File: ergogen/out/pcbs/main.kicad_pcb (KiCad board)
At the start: 2 copper layers, 95 x 76 mm, 42 parts

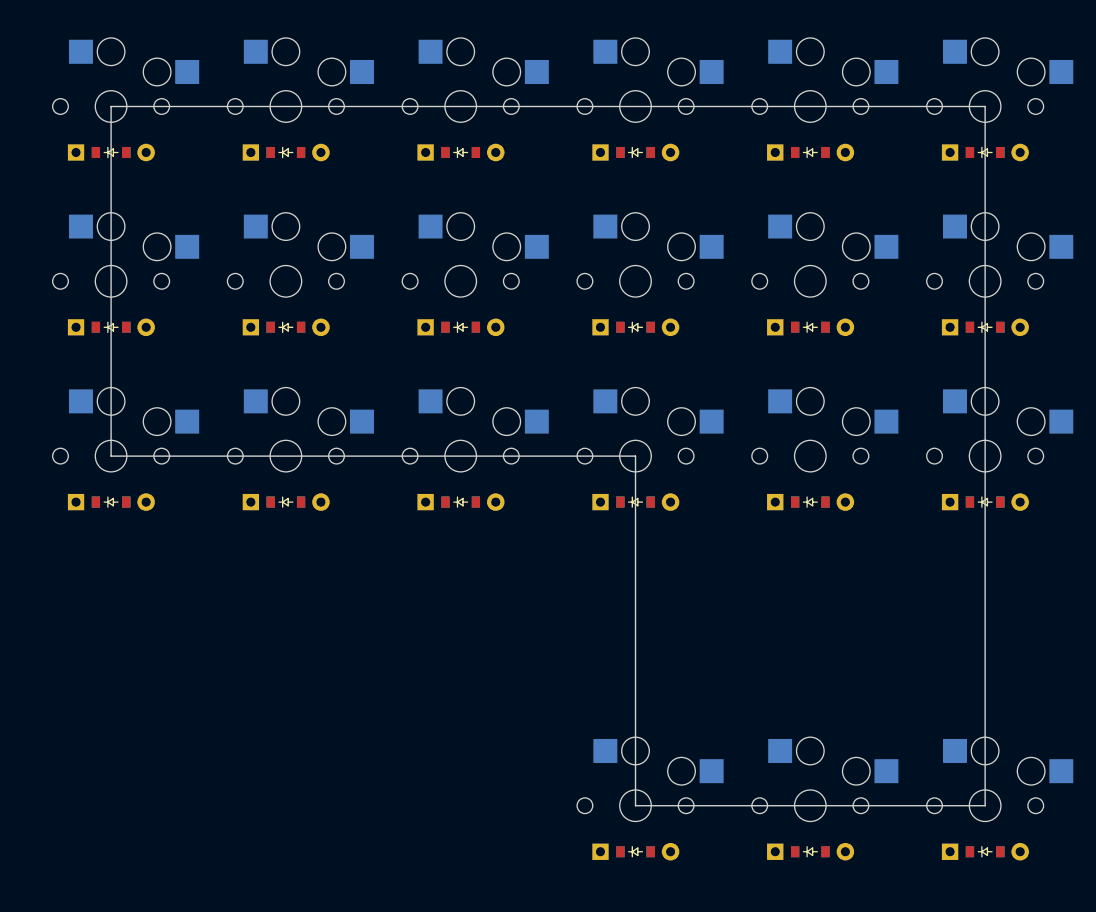
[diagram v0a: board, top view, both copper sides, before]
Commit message: feat: Improved outline padding.
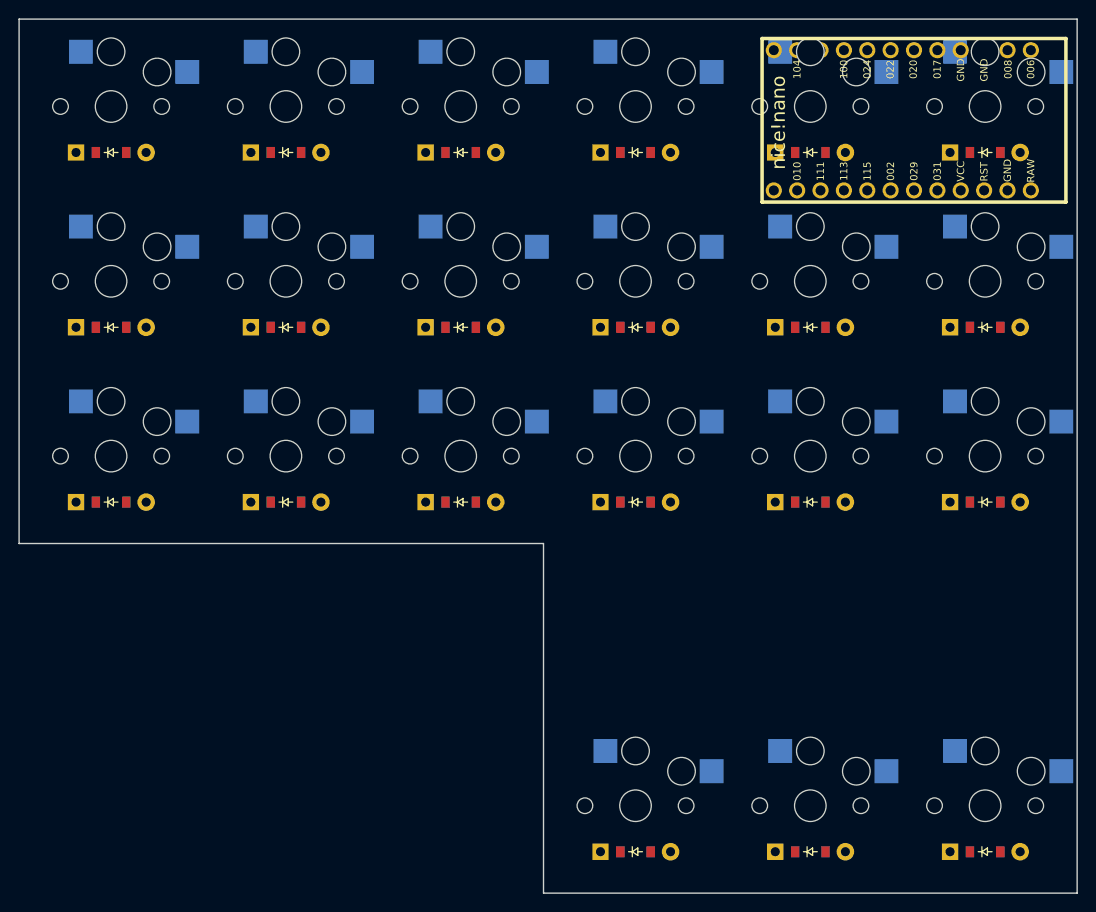
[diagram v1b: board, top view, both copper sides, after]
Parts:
- added MCU1: nice_nano, nice_nano, F.Cu at (86.0, -74.5)
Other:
- board size 95 x 76 mm -> 115 x 95 mm

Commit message: feat: Move diodes a little bit.
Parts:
- moved D1 2.00 mm to (2.00, -33.0)
- moved D10 2.00 mm to (59.0, 5.00)
- moved D11 2.00 mm to (59.0, -33.0)
- moved D12 2.00 mm to (59.0, -52.0)
- moved D13 2.00 mm to (59.0, -71.0)
- moved D14 2.00 mm to (78.0, 5.00)
- moved D15 2.00 mm to (78.0, -33.0)
- moved D16 2.00 mm to (78.0, -52.0)
- moved D17 2.00 mm to (78.0, -71.0)
- moved D18 2.00 mm to (97.0, 5.00)
- moved D19 2.00 mm to (97.0, -33.0)
- moved D2 2.00 mm to (2.00, -52.0)
- moved D20 2.00 mm to (97.0, -52.0)
- moved D21 2.00 mm to (97.0, -71.0)
- moved D3 2.00 mm to (2.00, -71.0)
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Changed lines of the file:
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@@
         )
     (module ComboDiode (layer F.Cu)
-        (at 0 -33 0)
+        (at 2 -33 0)
         (fp_text reference "D1" (at 0 0) (layer F.SilkS) hide (effects (font (size 1.27 1.27) (thickness 0.15))))
         (fp_text value "" (at 0 0) (layer F.SilkS) hide (effects (font (size 1.27 1.27) (thickness 0.15))))
@@
     )
     (module ComboDiode (layer F.Cu)
-        (at 0 -52 0)
+        (at 2 -52 0)
         (fp_text reference "D2" (at 0 0) (layer F.SilkS) hide (effects (font (size 1.27 1.27) (thickness 0.15))))
         (fp_text value "" (at 0 0) (layer F.SilkS) hide (effects (font (size 1.27 1.27) (thickness 0.15))))
@@
     )
     (module ComboDiode (layer F.Cu)
-        (at 0 -71 0)
+        (at 2 -71 0)
         (fp_text reference "D3" (at 0 0) (layer F.SilkS) hide (effects (font (size 1.27 1.27) (thickness 0.15))))
         (fp_text value "" (at 0 0) (layer F.SilkS) hide (effects (font (size 1.27 1.27) (thickness 0.15))))
@@
     )
     (module ComboDiode (layer F.Cu)
-        (at 19 -33 0)
+        (at 21 -33 0)
         (fp_text reference "D4" (at 0 0) (layer F.SilkS) hide (effects (font (size 1.27 1.27) (thickness 0.15))))
         (fp_text value "" (at 0 0) (layer F.SilkS) hide (effects (font (size 1.27 1.27) (thickness 0.15))))
@@
     )
     (module ComboDiode (layer F.Cu)
-        (at 19 -52 0)
+        (at 21 -52 0)
         (fp_text reference "D5" (at 0 0) (layer F.SilkS) hide (effects (font (size 1.27 1.27) (thickness 0.15))))
         (fp_text value "" (at 0 0) (layer F.SilkS) hide (effects (font (size 1.27 1.27) (thickness 0.15))))
@@
     )
     (module ComboDiode (layer F.Cu)
-        (at 19 -71 0)
+        (at 21 -71 0)
         (fp_text reference "D6" (at 0 0) (layer F.SilkS) hide (effects (font (size 1.27 1.27) (thickness 0.15))))
         (fp_text value "" (at 0 0) (layer F.SilkS) hide (effects (font (size 1.27 1.27) (thickness 0.15))))
@@
     )
     (module ComboDiode (layer F.Cu)
-        (at 38 -33 0)
+        (at 40 -33 0)
         (fp_text reference "D7" (at 0 0) (layer F.SilkS) hide (effects (font (size 1.27 1.27) (thickness 0.15))))
         (fp_text value "" (at 0 0) (layer F.SilkS) hide (effects (font (size 1.27 1.27) (thickness 0.15))))
@@
     )
     (module ComboDiode (layer F.Cu)
-        (at 38 -52 0)
+        (at 40 -52 0)
         (fp_text reference "D8" (at 0 0) (layer F.SilkS) hide (effects (font (size 1.27 1.27) (thickness 0.15))))
         (fp_text value "" (at 0 0) (layer F.SilkS) hide (effects (font (size 1.27 1.27) (thickness 0.15))))
@@
     )
     (module ComboDiode (layer F.Cu)
-        (at 38 -71 0)
+        (at 40 -71 0)
         (fp_text reference "D9" (at 0 0) (layer F.SilkS) hide (effects (font (size 1.27 1.27) (thickness 0.15))))
         (fp_text value "" (at 0 0) (layer F.SilkS) hide (effects (font (size 1.27 1.27) (thickness 0.15))))
@@
     )
     (module ComboDiode (layer F.Cu)
-        (at 57 5 0)
+        (at 59 5 0)
         (fp_text reference "D10" (at 0 0) (layer F.SilkS) hide (effects (font (size 1.27 1.27) (thickness 0.15))))
         (fp_text value "" (at 0 0) (layer F.SilkS) hide (effects (font (size 1.27 1.27) (thickness 0.15))))
@@
     )
     (module ComboDiode (layer F.Cu)
-        (at 57 -33 0)
+        (at 59 -33 0)
         (fp_text reference "D11" (at 0 0) (layer F.SilkS) hide (effects (font (size 1.27 1.27) (thickness 0.15))))
         (fp_text value "" (at 0 0) (layer F.SilkS) hide (effects (font (size 1.27 1.27) (thickness 0.15))))
@@
     )
     (module ComboDiode (layer F.Cu)
-        (at 57 -52 0)
+        (at 59 -52 0)
         (fp_text reference "D12" (at 0 0) (layer F.SilkS) hide (effects (font (size 1.27 1.27) (thickness 0.15))))
         (fp_text value "" (at 0 0) (layer F.SilkS) hide (effects (font (size 1.27 1.27) (thickness 0.15))))
@@
     )
     (module ComboDiode (layer F.Cu)
-        (at 57 -71 0)
+        (at 59 -71 0)
         (fp_text reference "D13" (at 0 0) (layer F.SilkS) hide (effects (font (size 1.27 1.27) (thickness 0.15))))
         (fp_text value "" (at 0 0) (layer F.SilkS) hide (effects (font (size 1.27 1.27) (thickness 0.15))))
@@
     )
     (module ComboDiode (layer F.Cu)
-        (at 76 5 0)
+        (at 78 5 0)
         (fp_text reference "D14" (at 0 0) (layer F.SilkS) hide (effects (font (size 1.27 1.27) (thickness 0.15))))
         (fp_text value "" (at 0 0) (layer F.SilkS) hide (effects (font (size 1.27 1.27) (thickness 0.15))))
@@
     )
     (module ComboDiode (layer F.Cu)
-        (at 76 -33 0)
+        (at 78 -33 0)
         (fp_text reference "D15" (at 0 0) (layer F.SilkS) hide (effects (font (size 1.27 1.27) (thickness 0.15))))
         (fp_text value "" (at 0 0) (layer F.SilkS) hide (effects (font (size 1.27 1.27) (thickness 0.15))))
@@
     )
     (module ComboDiode (layer F.Cu)
-        (at 76 -52 0)
+        (at 78 -52 0)
         (fp_text reference "D16" (at 0 0) (layer F.SilkS) hide (effects (font (size 1.27 1.27) (thickness 0.15))))
         (fp_text value "" (at 0 0) (layer F.SilkS) hide (effects (font (size 1.27 1.27) (thickness 0.15))))
@@
     )
     (module ComboDiode (layer F.Cu)
-        (at 76 -71 0)
+        (at 78 -71 0)
         (fp_text reference "D17" (at 0 0) (layer F.SilkS) hide (effects (font (size 1.27 1.27) (thickness 0.15))))
         (fp_text value "" (at 0 0) (layer F.SilkS) hide (effects (font (size 1.27 1.27) (thickness 0.15))))
@@
     )
     (module ComboDiode (layer F.Cu)
-        (at 95 5 0)
+        (at 97 5 0)
         (fp_text reference "D18" (at 0 0) (layer F.SilkS) hide (effects (font (size 1.27 1.27) (thickness 0.15))))
         (fp_text value "" (at 0 0) (layer F.SilkS) hide (effects (font (size 1.27 1.27) (thickness 0.15))))
@@
     )
     (module ComboDiode (layer F.Cu)
-        (at 95 -33 0)
+        (at 97 -33 0)
         (fp_text reference "D19" (at 0 0) (layer F.SilkS) hide (effects (font (size 1.27 1.27) (thickness 0.15))))
         (fp_text value "" (at 0 0) (layer F.SilkS) hide (effects (font (size 1.27 1.27) (thickness 0.15))))
@@
     )
     (module ComboDiode (layer F.Cu)
-        (at 95 -52 0)
+        (at 97 -52 0)
         (fp_text reference "D20" (at 0 0) (layer F.SilkS) hide (effects (font (size 1.27 1.27) (thickness 0.15))))
         (fp_text value "" (at 0 0) (layer F.SilkS) hide (effects (font (size 1.27 1.27) (thickness 0.15))))
@@
     )
     (module ComboDiode (layer F.Cu)
-        (at 95 -71 0)
+        (at 97 -71 0)
         (fp_text reference "D21" (at 0 0) (layer F.SilkS) hide (effects (font (size 1.27 1.27) (thickness 0.15))))
         (fp_text value "" (at 0 0) (layer F.SilkS) hide (effects (font (size 1.27 1.27) (thickness 0.15))))

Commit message: feat: Shift nice nano to the empty row.
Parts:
- moved MCU1 55.5 mm to (87.0, -19.0)

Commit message: feat: Add battery jack.
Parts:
- added JST1: , JST_PH_S2B-PH-K_02x2.00mm_Angled, F.Cu at (62.0, -23.0)
- moved MCU1 1.41 mm to (86.0, -18.0)
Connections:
- D1 pad 1: P002 -> P017
- D10 pad 1: P113 -> P010
- D11 pad 1: P002 -> P017
- D12 pad 1: P029 -> P020
- D13 pad 1: P031 -> P022
- D14 pad 1: P113 -> P010
- D15 pad 1: P002 -> P017
- D16 pad 1: P029 -> P020
- D17 pad 1: P031 -> P022
- D18 pad 1: P113 -> P010
- D19 pad 1: P002 -> P017
- D2 pad 1: P029 -> P020
- D20 pad 1: P029 -> P020
- D21 pad 1: P031 -> P022
- D3 pad 1: P031 -> P022
- D4 pad 1: P002 -> P017
- D5 pad 1: P029 -> P020
- D6 pad 1: P031 -> P022
- D7 pad 1: P002 -> P017
- D8 pad 1: P029 -> P020
- D9 pad 1: P031 -> P022
- S1 pad 1: P020 -> P031
- S10 pad 1: P100 -> P115
- S11 pad 1: P100 -> P115
- S12 pad 1: P100 -> P115
- S13 pad 1: P100 -> P115
- S14 pad 1: P011 -> P113
- S15 pad 1: P011 -> P113
- S16 pad 1: P011 -> P113
- S17 pad 1: P011 -> P113
- S18 pad 1: P017 -> P111
- S19 pad 1: P017 -> P111
- S2 pad 1: P020 -> P031
- S20 pad 1: P017 -> P111
- S21 pad 1: P017 -> P111
- S3 pad 1: P020 -> P031
- S4 pad 1: P022 -> P029
- S5 pad 1: P022 -> P029
- S6 pad 1: P022 -> P029
- S7 pad 1: P024 -> P002
- S8 pad 1: P024 -> P002
- S9 pad 1: P024 -> P002

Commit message: feat: Add reset switch.
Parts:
- added B1: Panasonic_EVQPUL_EVQPUC, Panasonic_EVQPUL_EVQPUC, F.Cu at (49.0, -16.0)
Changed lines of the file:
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@@
         (pad 2 thru_hole oval (at 1 0 -90) (size 1.2 1.7) (drill 0.75) (layers *.Cu *.Mask) (net 33 "GND"))
+    )
+    (module Panasonic_EVQPUL_EVQPUC (layer F.Cu)
+        (descr "http://industrial.panasonic.com/cdbs/www-data/pdf/ATV0000/ATV0000CE5.pdf")
+        (tags "SMD SMT SPST EVQPUL EVQPUC")
+        (at 49 -16 90)
+        (fp_text reference "B1" (at 0 0) (layer "F.SilkS") hide (effects (font (size 1 1) (thickness 0.15))))
+        (fp_text value "Panasonic_EVQPUL_EVQPUC" (at 0 3.5) (layer "F.Fab") hide (effects (font (size 1 1) (thickness 0.15))))
+        (fp_line (start -2.45 0.275) (end -2.45 -0.275) (stroke (width 0.12) (type solid)) (layer "B.SilkS"))
+        (fp_line (start -1.425 -1.85) (end -2.35 -1.85) (stroke (width 0.12) (type solid)) (layer "B.SilkS"))
+        (fp_line (start 2.35 -1.85) (end 1.425 -1.85) (stroke (width 0.12) (type solid)) (layer "B.SilkS"))
+        (fp_line (start 2.35 1.85) (end -2.35 1.85) (stroke (width 0.12) (type solid)) (layer "B.SilkS"))
+        (fp_line (start 2.45 0.275) (end 2.45 -0.275) (stroke (width 0.12) (type solid)) (layer "B.SilkS"))
+        (fp_line (start -3.9 2.25) (end -3.9 -3.25) (stroke (width 0.05) (type solid)) (layer "B.CrtYd"))
+        (fp_line (start 3.9 -3.25) (end -3.9 -3.25) (stroke (width 0.05) (type solid)) (layer "B.CrtYd"))
+        (fp_line (start 3.9 2.25) (end -3.9 2.25) (stroke (width 0.05) (type solid)) (layer "B.CrtYd"))
+        (fp_line (start 3.9 2.25) (end 3.9 -3.25) (stroke (width 0.05) (type solid)) (layer "B.CrtYd"))
+        (fp_line (start -2.35 1.75) (end -2.35 -1.75) (stroke (width 0.1) (type solid)) (layer "B.Fab"))
+        (fp_line (start -1.3 -2.75) (end -1.3 -1.75) (stroke (width 0.1) (type solid)) (layer "B.Fab"))
+        (fp_line (start 1.3 -2.75) (end -1.3 -2.75) (stroke (width 0.1) (type solid)) (layer "B.Fab"))
+        (fp_line (start 1.3 -2.75) (end 1.3 -1.75) (stroke (width 0.1) (type solid)) (layer "B.Fab"))
+        (fp_line (start 2.35 -1.75) (end -2.35 -1.75) (stroke (width 0.1) (type solid)) (layer "B.Fab"))
+        (fp_line (start 2.35 1.75) (end -2.35 1.75) (stroke (width 0.1) (type solid)) (layer "B.Fab"))
+        (fp_line (start 2.35 1.75) (end 2.35 -1.75) (stroke (width 0.1) (type solid)) (layer "B.Fab"))
+        (pad "" np_thru_hole circle (at 0 -1.375 90) (size 0.75 0.75) (drill 0.75) (layers "*.Cu" "*.Mask"))
+        (pad "" np_thru_hole circle (at 0 1.375 90) (size 0.75 0.75) (drill 0.75) (layers "*.Cu" "*.Mask"))
+        (pad "1" smd rect (at -2.625 -0.85 90) (size 1.55 1) (layers "B.Cu" "B.Paste" "B.Mask") (net 33 "GND"))
+        (pad "1" smd rect (at 2.625 -0.85 90) (size 1.55 1) (layers "B.Cu" "B.Paste" "B.Mask") (net 33 "GND"))
+        (pad "2" smd rect (at -2.625 0.85 90) (size 1.55 1) (layers "B.Cu" "B.Paste" "B.Mask") (net 34 "RST"))
+        (pad "2" smd rect (at 2.625 0.85 90) (size 1.55 1) (layers "B.Cu" "B.Paste" "B.Mask") (net 34 "RST"))
     )
   (gr_line (start -10 -85.5) (end 105 -85.5) (angle 90) (layer Edge.Cuts) (width 0.15))

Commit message: feat: Add battery switch
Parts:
- added T1: , E73:SPDT_C128955, F.Cu at (49.0, -24.0)
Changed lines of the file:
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@@
         (pad "2" smd rect (at 2.625 0.85 90) (size 1.55 1) (layers "B.Cu" "B.Paste" "B.Mask") (net 34 "RST"))
     )
+        (module E73:SPDT_C128955 (layer F.Cu)
+            (at 49 -24 90)
+            (fp_text reference "T1" (at 0 0) (layer F.SilkS) hide (effects (font (size 1.27 1.27) (thickness 0.15))))
+            (fp_text value "" (at 0 0) (layer F.SilkS) hide (effects (font (size 1.27 1.27) (thickness 0.15))))
+            (fp_line (start 1.95 -1.35) (end -1.95 -1.35) (layer B.SilkS) (width 0.15))
+            (fp_line (start 0 -1.35) (end -3.3 -1.35) (layer B.SilkS) (width 0.15))
+            (fp_line (start -3.3 -1.35) (end -3.3 1.5) (layer B.SilkS) (width 0.15))
+            (fp_line (start -3.3 1.5) (end 3.3 1.5) (layer B.SilkS) (width 0.15))
+            (fp_line (start 3.3 1.5) (end 3.3 -1.35) (layer B.SilkS) (width 0.15))
+            (fp_line (start 0 -1.35) (end 3.3 -1.35) (layer B.SilkS) (width 0.15))
+            (fp_line (start -1.95 -3.85) (end 1.95 -3.85) (layer Dwgs.User) (width 0.15))
+            (fp_line (start 1.95 -3.85) (end 1.95 -1.35) (layer Dwgs.User) (width 0.15))
+            (fp_line (start -1.95 -1.35) (end -1.95 -3.85) (layer Dwgs.User) (width 0.15))
+            (pad "" np_thru_hole circle (at 1.5 0) (size 1 1) (drill 0.9) (layers *.Cu *.Mask))
+            (pad "" np_thru_hole circle (at -1.5 0) (size 1 1) (drill 0.9) (layers *.Cu *.Mask))
+            (pad 1 smd rect (at -2.25 2.075 90) (size 0.9 1.25) (layers B.Cu B.Paste B.Mask) (net 44 "pos"))
+            (pad 2 smd rect (at 0.75 2.075 90) (size 0.9 1.25) (layers B.Cu B.Paste B.Mask) (net 32 "RAW"))
+            (pad 3 smd rect (at 2.25 2.075 90) (size 0.9 1.25) (layers B.Cu B.Paste B.Mask))
+            (pad "" smd rect (at 3.7 -1.1 90) (size 0.9 0.9) (layers B.Cu B.Paste B.Mask))
+            (pad "" smd rect (at 3.7 1.1 90) (size 0.9 0.9) (layers B.Cu B.Paste B.Mask))
+            (pad "" smd rect (at -3.7 1.1 90) (size 0.9 0.9) (layers B.Cu B.Paste B.Mask))
+            (pad "" smd rect (at -3.7 -1.1 90) (size 0.9 0.9) (layers B.Cu B.Paste B.Mask))
+        )
   (gr_line (start -10 -85.5) (end 105 -85.5) (angle 90) (layer Edge.Cuts) (width 0.15))
 (gr_line (start -10 -85.5) (end -10 -28.5) (angle 90) (layer Edge.Cuts) (width 0.15))

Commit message: feat: Finished left side.
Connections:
- D1 pad 1: P017 -> P011
- D11 pad 1: P017 -> P011
- D12 pad 1: P020 -> P100
- D13 pad 1: P022 -> P024
- D15 pad 1: P017 -> P011
- D16 pad 1: P020 -> P100
- D17 pad 1: P022 -> P024
- D19 pad 1: P017 -> P011
- D2 pad 1: P020 -> P100
- D20 pad 1: P020 -> P100
- D21 pad 1: P022 -> P024
- D3 pad 1: P022 -> P024
- D4 pad 1: P017 -> P011
- D5 pad 1: P020 -> P100
- D6 pad 1: P022 -> P024
- D7 pad 1: P017 -> P011
- D8 pad 1: P020 -> P100
- D9 pad 1: P022 -> P024
- S1 pad 1: P031 -> P022
- S10 pad 1: P115 -> P113
- S11 pad 1: P115 -> P113
- S12 pad 1: P115 -> P113
- S13 pad 1: P115 -> P113
- S14 pad 1: P113 -> P111
- S15 pad 1: P113 -> P111
- S16 pad 1: P113 -> P111
- S17 pad 1: P113 -> P111
- S18 pad 1: P111 -> P115
- S19 pad 1: P111 -> P115
- S2 pad 1: P031 -> P022
- S20 pad 1: P111 -> P115
- S21 pad 1: P111 -> P115
- S3 pad 1: P031 -> P022
- S4 pad 1: P029 -> P020
- S5 pad 1: P029 -> P020
- S6 pad 1: P029 -> P020
- S7 pad 1: P002 -> P017
- S8 pad 1: P002 -> P017
- S9 pad 1: P002 -> P017

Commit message: feat: Shift PCB within KiCad
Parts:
- moved B1 180.3 mm to (149.0, 134.0)
- moved D1 180.3 mm to (102.0, 117.0)
- moved D10 180.3 mm to (159.0, 155.0)
- moved D11 180.3 mm to (159.0, 117.0)
- moved D12 180.3 mm to (159.0, 98.0)
- moved D13 180.3 mm to (159.0, 79.0)
- moved D14 180.3 mm to (178.0, 155.0)
- moved D15 180.3 mm to (178.0, 117.0)
- moved D16 180.3 mm to (178.0, 98.0)
- moved D17 180.3 mm to (178.0, 79.0)
- moved D18 180.3 mm to (197.0, 155.0)
- moved D19 180.3 mm to (197.0, 117.0)
- moved D2 180.3 mm to (102.0, 98.0)
- moved D20 180.3 mm to (197.0, 98.0)
- moved D21 180.3 mm to (197.0, 79.0)
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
